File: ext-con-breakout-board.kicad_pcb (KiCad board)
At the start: 2 copper layers, 25 x 16 mm, 6 parts, among them J1 Conn_02x12_Odd_Even, J2 Conn_01x03, J3 Conn_01x03, J4 Conn_01x03, J5 Conn_01x05, J6 Conn_01x03

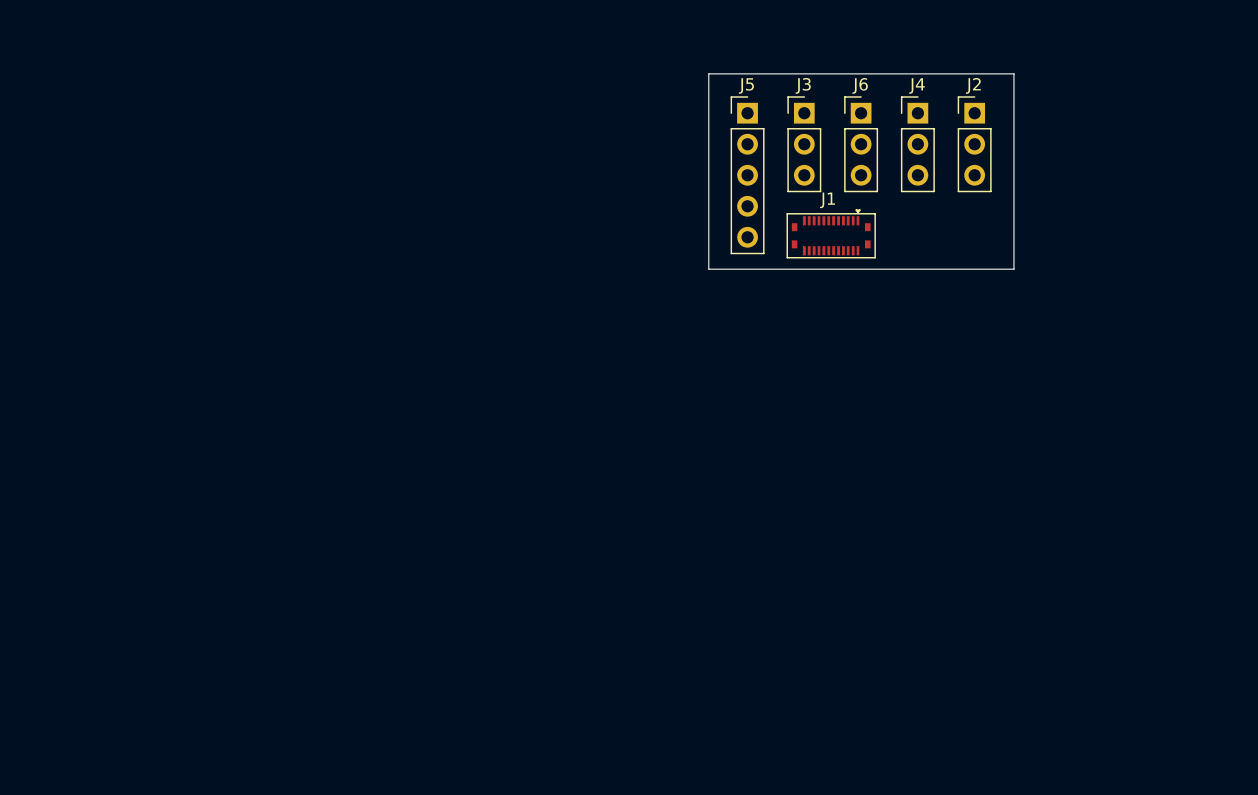
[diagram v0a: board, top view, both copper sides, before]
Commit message: Begin fanning out the nets near the FPC connector
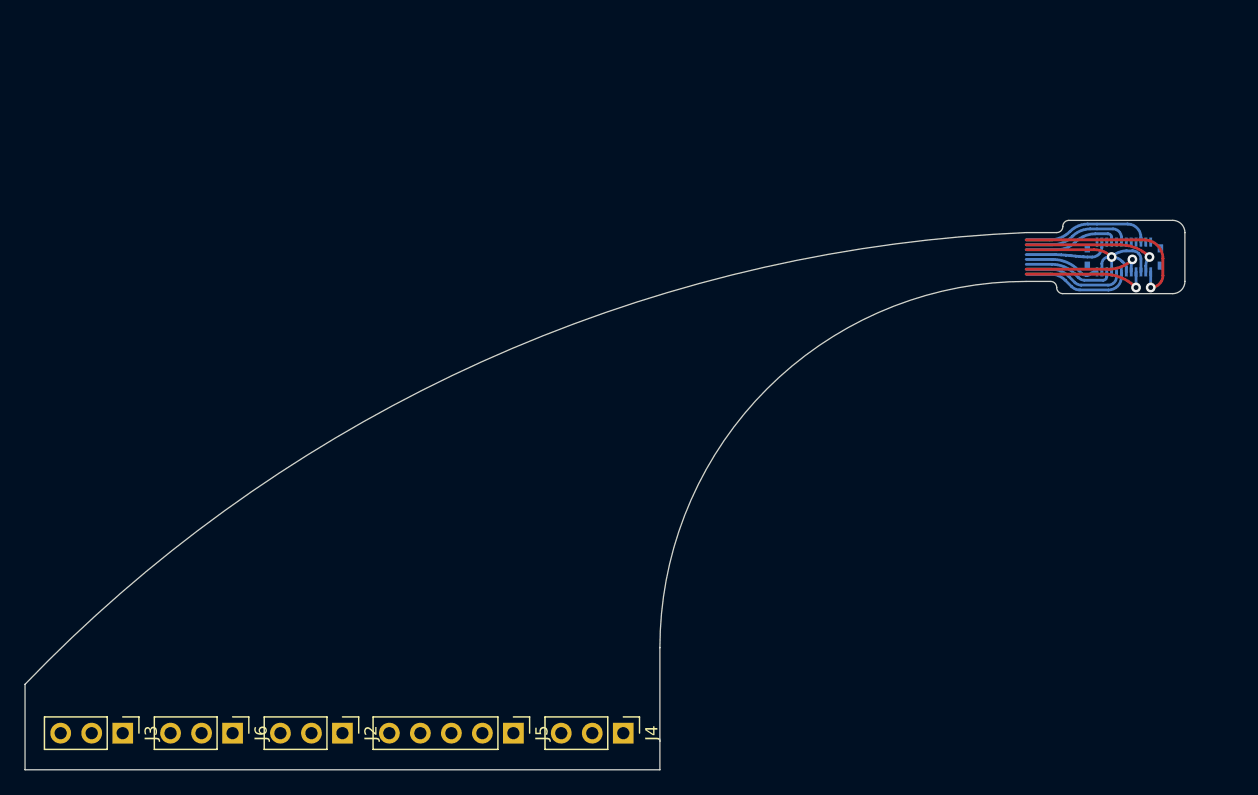
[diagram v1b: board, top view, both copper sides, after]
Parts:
- J1: moved to B.Cu
- moved J3 75.5 mm to (89.0, 143.0), turned to -90 degrees
- moved J2 72.5 mm to (107.0, 143.0), turned to -90 degrees
- moved J6 72.3 mm to (98.0, 143.0), turned to -90 degrees
- moved J4 56.2 mm to (130.0, 143.0), turned to -90 degrees
- moved J5 54.3 mm to (121.0, 143.0), turned to -90 degrees
- moved J1 24.0 mm to (171.0, 104.0)
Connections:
- J2 pad 1: +1V8 -> GND
- J2 pad 3: GND -> +1V8
- J3 pad 1: /I2C4_SDA -> GND
- J3 pad 3: GND -> /I2C4_SDA
- J4 pad 1: /UART1_RXD -> GND
- J4 pad 2: /UART1_TXD -> /UART1_RXD
- J4 pad 3: GND -> /UART1_TXD
- J5 pad 1: /SPI_SS1 -> GND
- J5 pad 2: /SPI_SCK -> /SPI_SS1
- J5 pad 3: /SPI_MOSI -> /SPI_SCK
- J5 pad 4: /SPI_MISO -> /SPI_MOSI
- J5 pad 5: GND -> /SPI_MISO
- J6 pad 1: /GPIO4_IO28 -> GND
- J6 pad 3: GND -> /GPIO4_IO28
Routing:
- net /I2C4_SDA: track 0.00 -> 16.2 mm, vias 0 -> 1
- net GND: track 0.00 -> 16.0 mm, vias 0 -> 1
- net /I2C4_SCL: track 0.00 -> 11.7 mm, vias 0 -> 1
- net /GPIO4_IO28: track 0.00 -> 10.7 mm
- net /UART1_RXD: track 0.00 -> 10.6 mm, vias 0 -> 1
- net /UART1_TXD: track 0.00 -> 9.95 mm, vias 0 -> 1
- net /SPI_SS1: track 0.00 -> 9.18 mm
- net /GPIO4_IO11: track 0.00 -> 8.87 mm
- net /SPI_SCK: track 0.00 -> 8.56 mm
- net +1V8: track 0.00 -> 7.86 mm
- net /SPI_MOSI: track 0.00 -> 7.52 mm
- net +3V3: track 0.00 -> 7.06 mm
- net /SPI_MISO: track 0.00 -> 6.25 mm
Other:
- board size 25 x 16 mm -> 95 x 45 mm

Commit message: Adjust the edge cuts based on the space available on the phone
Rev v1.0.6 of the phone has a plastic bracket on the mid-frame which
joins the WiFi tab holder section to the section above the smartcard
slot. This piece bridges over the testi points and has holes where the
test points are located.

The intent of the edge cut design in this commit is to snake around the
plastic mid-frame that bridges between the two sections as was
described. If successful, this will neatly fit in the space remaining on
a v1.0.6 phone.

Also begin routing in this allotted space which tries to avoid the
plastic obstructions. Since avoiding the plastic brakets requires the
use of non-45 degree angles, this commit requires adjusting the end
points of the traces by hand with the use of some simple trig
calculations along with having to join some tracks with fillets in order
to accomplish the desired arc radii.

Tear drops are used in this commit thanks to NilujePerchut's handy
script (on commit 41c055d of the kicad_scripts repo).
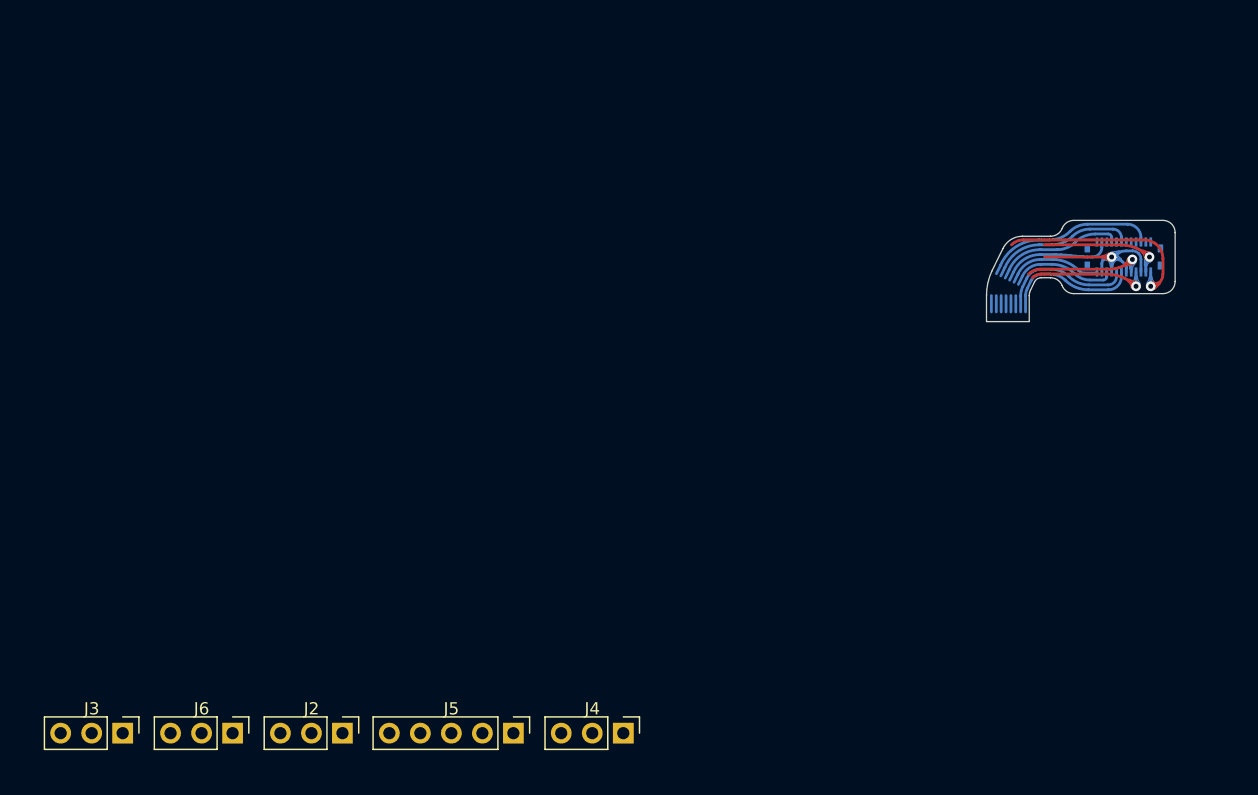
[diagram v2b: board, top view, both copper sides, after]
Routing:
- net /GPIO4_IO28: track 10.7 -> 15.7 mm
- net /GPIO4_IO11: track 8.87 -> 13.4 mm
- net +1V8: track 7.86 -> 11.9 mm
- net +3V3: track 7.06 -> 10.7 mm
- net /SPI_MISO: track 6.25 -> 9.34 mm
- net /SPI_SCK: track 8.56 -> 11.5 mm
- net /SPI_MOSI: track 7.52 -> 10.2 mm
- net /SPI_SS1: track 9.18 -> 11.5 mm
- net GND: track 16.0 -> 14.4 mm
- net /I2C4_SCL: track 11.7 -> 10.2 mm
- net /I2C4_SDA: track 16.2 -> 17.3 mm
- net /UART1_RXD: track 10.6 -> 10.0 mm
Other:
- board size 95 x 45 mm -> 15.4 x 8.3 mm

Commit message: Route the remaining portion of the FPC section and add the rigid section
The rigid section has a mounting hole which lines up with the center
screw that holds the M.2 cover in place. This will allow the board to be
mounted to the back of the phone.

Extra flex length was given to ensure enough distance to reach the
position where the rigid section will be mounted. The drawings on the
User.1 layer shows where the plastic obstacles are as well as the
location of the M1.4 threaded hole. There is approximately 5.4mm of
additional slack in the length of the flex section so that it can be
tucked inside the volume it runs along.

The rigid section of the board will sit between the M.2 modules, on top
of the ~10.5mm plastic section that separates the two. The rigid section
has a 7mm and should close to the center of the plastic divider.
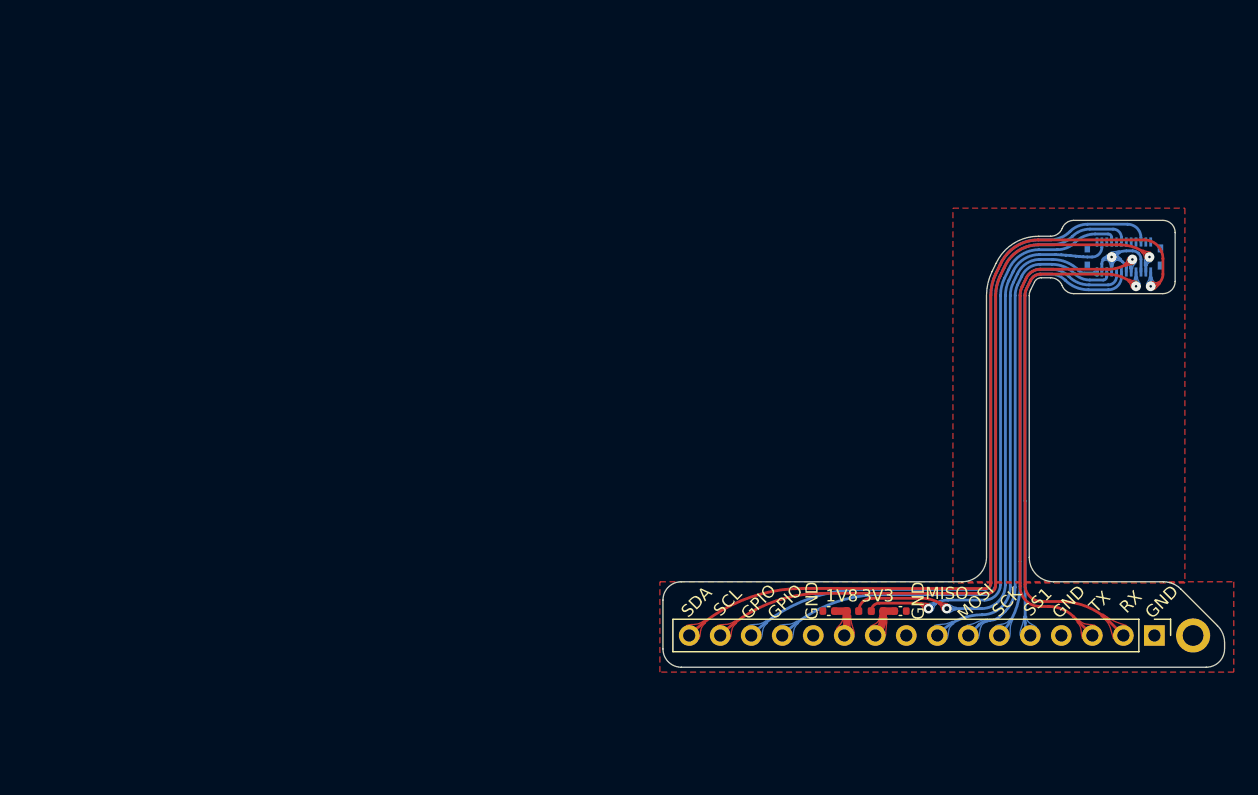
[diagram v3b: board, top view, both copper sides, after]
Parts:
- removed J3, J4, J6: Conn_01x03, Connector_PinHeader_2.54mm:PinHeader_1x03_P2.54mm_Vertical
- removed J5: Conn_01x05, Connector_PinHeader_2.54mm:PinHeader_1x05_P2.54mm_Vertical
- added C1: 100nF, Capacitor_SMD:C_0402_1005Metric, F.Cu at (152.7, 133.0)
- added C2: 100nF, Capacitor_SMD:C_0402_1005Metric, F.Cu at (146.8, 133.0)
- added FB1: FerriteBead_Small, Inductor_SMD:L_0402_1005Metric, F.Cu at (150.8, 133.0)
- added FB2: FerriteBead_Small, Inductor_SMD:L_0402_1005Metric, F.Cu at (148.8, 133.0)
- added H1: MountingHole_Pad, ext-con-breakout-board:MountingHole_1.7mm_M1.4_Pad, F.Cu at (176.7, 135.0)
- J2: value Conn_01x03 -> Conn_01x16; footprint Connector_PinHeader_2.54mm:PinHeader_1x03_P2.54mm_Vertical -> Connector_PinHeader_2.54mm:PinHeader_1x16_P2.54mm_Vertical
- moved J2 67.0 mm to (173.5, 135.0)
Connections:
- J2 pad 2: +3V3 -> /UART1_RXD
- J2 pad 3: +1V8 -> /UART1_TXD
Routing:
- net /I2C4_SCL: track 10.2 -> 64.1 mm
- net /I2C4_SDA: track 17.3 -> 71.0 mm
- net /GPIO4_IO28: track 15.7 -> 60.6 mm
- net /GPIO4_IO11: track 13.4 -> 56.2 mm
- net +3V3: track 10.7 -> 48.2 mm, vias 0 -> 1
- net +1V8: track 11.9 -> 47.7 mm, vias 0 -> 1
- net /UART1_RXD: track 10.0 -> 44.9 mm
- net /UART1_TXD: track 9.85 -> 43.2 mm
- net /SPI_MISO: track 9.34 -> 40.7 mm
- net /SPI_MOSI: track 10.2 -> 39.6 mm
- net /SPI_SCK: track 11.5 -> 38.5 mm
- net /SPI_SS1: track 11.5 -> 38.2 mm
- net GND: track 14.4 -> 8.88 mm
- net Net-(C2-Pad1): track 0.00 -> 3.16 mm
- net Net-(C1-Pad1): track 0.00 -> 3.10 mm
- added copper zone on F.Cu, net GND
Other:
- board size 15.4 x 8.3 mm -> 46 x 36.6 mm
- board text added: "1V8"
- board text added: "3V3"
- board text added: "EXT CON Breakout Board v0.5"
- board text added: "GND"
- board text added: "GPIO"
- board text added: "MISO"
- board text added: "MOSI"
- board text added: "Purism SPC GPLv3+"
- board text added: "RX"
- board text added: "SCK"
- board text added: "SCL"
- board text added: "SDA"
- board text added: "SS1"
- board text added: "TX"

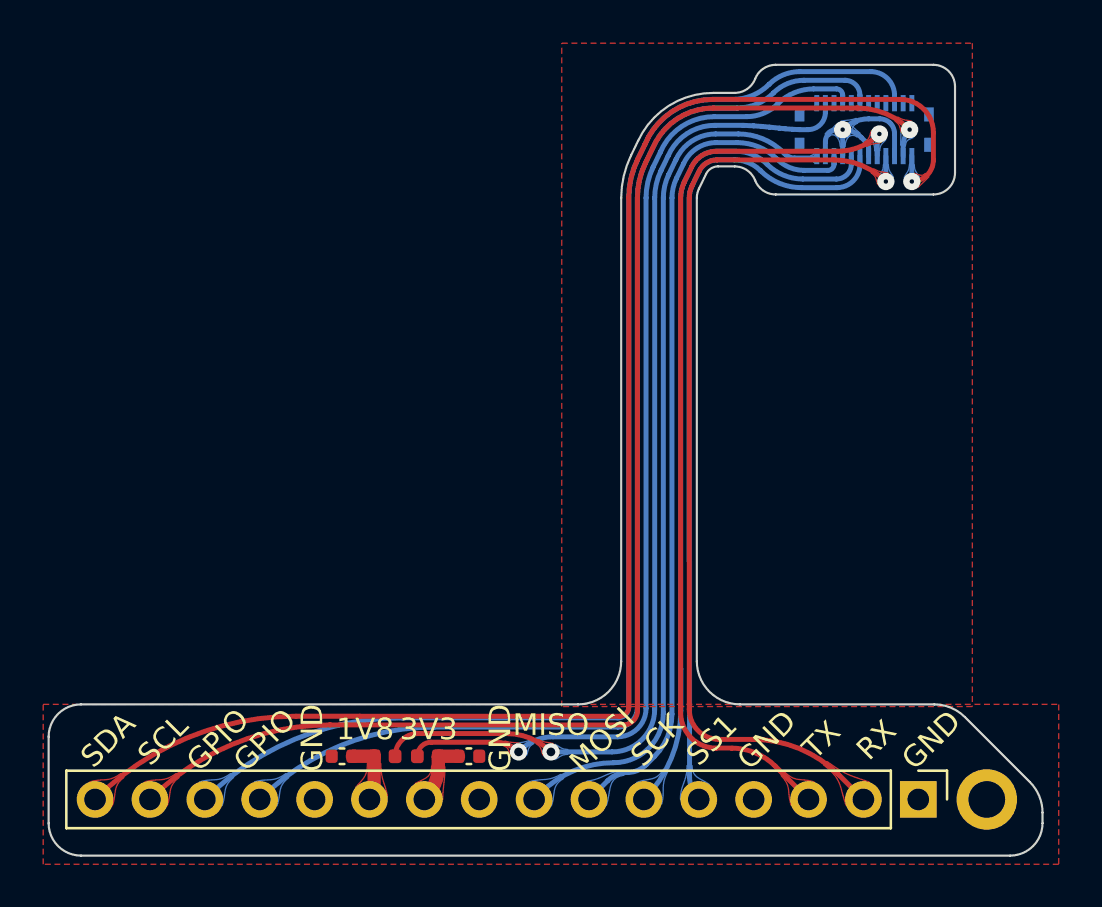
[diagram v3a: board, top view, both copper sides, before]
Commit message: Make the board 4 layers and move the flex copper to the inner layers
The 0402 caps and ferrite beads and their traces have to remain on the
F.Cu layer.

This commit was accomplished by having to manually edit the .kicad_pcb
text file in order to move the previous F.Cu & B.Cu layers to becoming
In1.Cu & In2.Cu.

Also add notes regarding where the rigid section is, where the flex
section is, and that the area with the FPC connector should have a
kapton stiffener placed there. These notes are found on the
User.Comments layer.
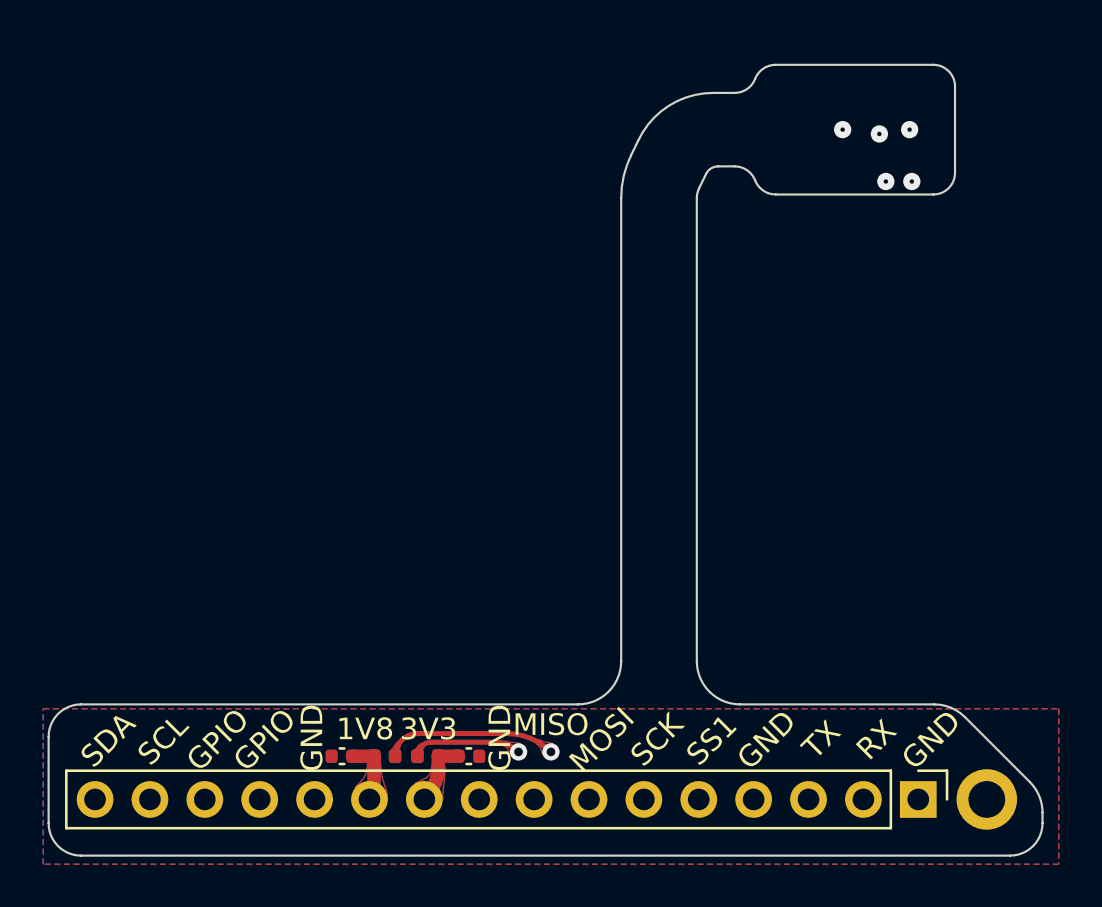
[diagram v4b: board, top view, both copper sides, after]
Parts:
- J1: moved to F.Cu
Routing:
- added copper zone on B.Cu, net GND
- added copper zone on In1.Cu, net GND
- added copper zone on In2.Cu, net GND
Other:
- copper layers 2 -> 4
- board text added: "Flex Section"
- board text added: "Kapton Stiffener"
- board text added: "Rigid Section"
